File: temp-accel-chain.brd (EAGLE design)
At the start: 29.8 x 10.5 mm, 8 parts, among them U1 ADT7420UCPZ-R2

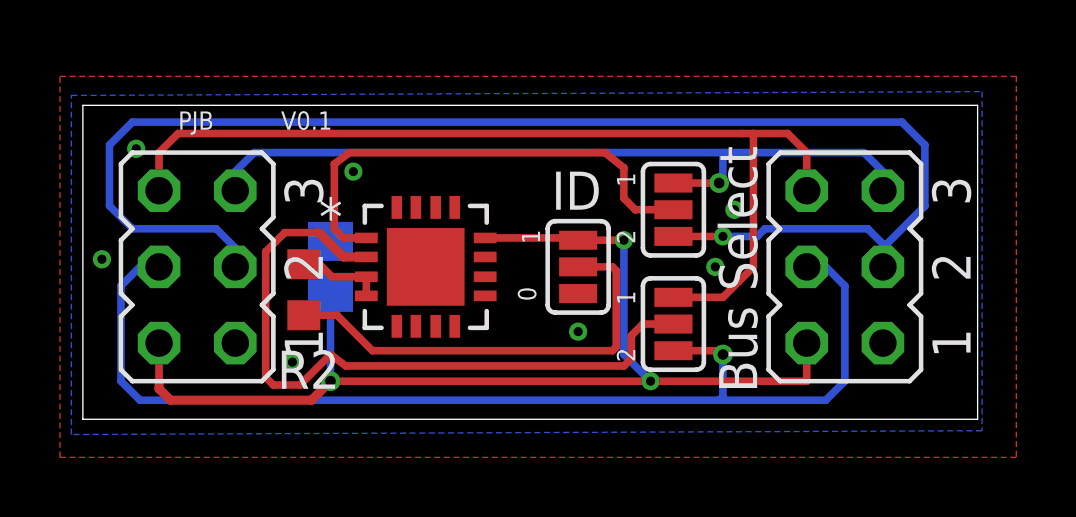
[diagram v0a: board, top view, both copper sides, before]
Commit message: added accel to back and mostly routed
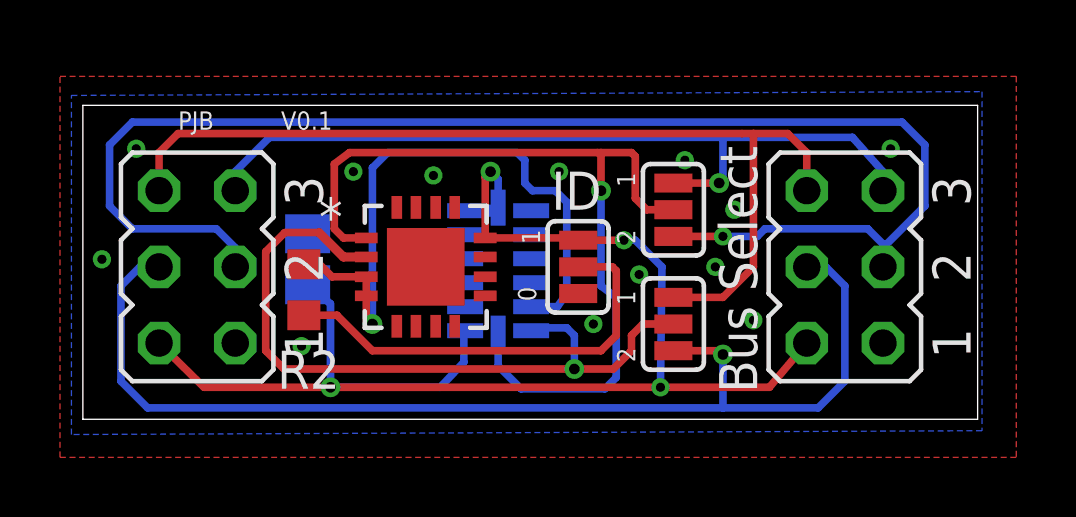
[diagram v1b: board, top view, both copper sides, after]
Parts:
- added U2: ADXL345, SparkFun-Sensors:LGA14
- moved C1 0.80 mm to (8.76, 5.33)
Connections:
- net ADD: now also U2.12
- net GND: now also U2.2, U2.4, U2.5
- net SCL: now also U2.14
- net SDA: now also U2.13
- net VCC: now also U2.1, U2.6, U2.7
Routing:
- net ADD: track 2.89 -> 21.4 mm, vias 0 -> 1
- net SCL: track 16.1 -> 29.6 mm, vias 0 -> 1
- net VCC: track 37.5 -> 47.7 mm, vias 3 -> 4
- net SDA: track 23.4 -> 24.7 mm, vias 0 -> 1
- net SCL1: track 26.0 -> 26.9 mm

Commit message: completely routed board
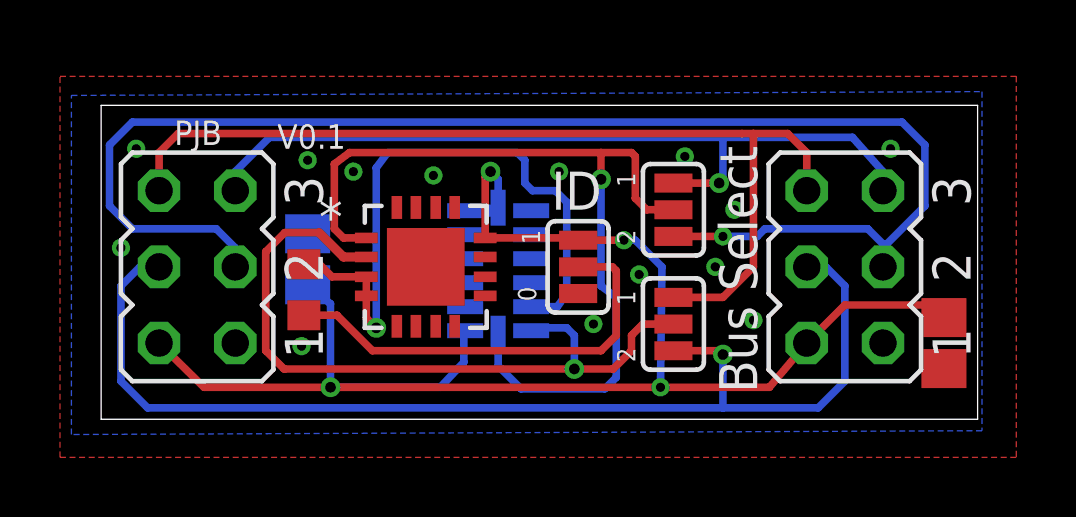
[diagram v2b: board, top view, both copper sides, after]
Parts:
- added C2: (no value), resistor:C0805
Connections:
- net GND: now also C2.2
- net VCC: now also C2.1
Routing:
- net VCC: track 47.7 -> 53.3 mm
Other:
- board size 29.8 x 10.5 mm -> 29.2 x 10.5 mm
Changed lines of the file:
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@@
 <setting verticaltext="up"/>
 </settings>
-<grid distance="5" unitdist="mil" unit="mil" style="lines" multiple="1" display="no" altdistance="1" altunitdist="mil" altunit="mil"/>
+<grid distance="5" unitdist="mil" unit="mm" style="lines" multiple="1" display="no" altdistance="1" altunitdist="mil" altunit="mil"/>
 <layers>
 <layer number="1" name="Top" color="4" fill="1" visible="yes" active="yes"/>
@@
 <layer number="21" name="tPlace" color="7" fill="1" visible="no" active="yes"/>
 <layer number="22" name="bPlace" color="7" fill="1" visible="yes" active="yes"/>
-<layer number="23" name="tOrigins" color="15" fill="1" visible="no" active="yes"/>
+<layer number="23" name="tOrigins" color="15" fill="1" visible="yes" active="yes"/>
 <layer number="24" name="bOrigins" color="15" fill="1" visible="yes" active="yes"/>
-<layer number="25" name="tNames" color="7" fill="1" visible="no" active="yes"/>
+<layer number="25" name="tNames" color="7" fill="1" visible="yes" active="yes"/>
 <layer number="26" name="bNames" color="7" fill="1" visible="yes" active="yes"/>
-<layer number="27" name="tValues" color="7" fill="1" visible="no" active="yes"/>
+<layer number="27" name="tValues" color="7" fill="1" visible="yes" active="yes"/>
 <layer number="28" name="bValues" color="7" fill="1" visible="yes" active="yes"/>
 <layer number="29" name="tStop" color="7" fill="3" visible="no" active="yes"/>
@@
 <board>
 <plain>
-<wire x1="1.27" y1="0" x2="31.095" y2="0" width="0" layer="20"/>
+<wire x1="1.8796" y1="0" x2="31.095" y2="0" width="0" layer="20"/>
 <wire x1="31.095" y1="0" x2="31.095" y2="10.465" width="0" layer="20"/>
-<wire x1="31.095" y1="10.465" x2="1.27" y2="10.465" width="0" layer="20"/>
-<wire x1="1.27" y1="10.465" x2="1.27" y2="0" width="0" layer="20"/>
+<wire x1="31.095" y1="10.465" x2="1.8796" y2="10.465" width="0" layer="20"/>
+<wire x1="1.8796" y1="10.465" x2="1.8796" y2="0" width="0" layer="20"/>
 <text x="23.749" y="0.889" size="1.27" layer="25" rot="R90">Bus Select</text>
 <text x="19.685" y="3.81" size="0.6096" layer="25" rot="R90">1</text>
@@
 <text x="16.383" y="3.937" size="0.6096" layer="25" rot="R90">0</text>
 <text x="16.51" y="5.842" size="0.6096" layer="25" rot="R90">1</text>
-<text x="4.445" y="9.652" size="0.6096" layer="25">PJB</text>
-<text x="7.874" y="9.652" size="0.6096" layer="25">V0.1</text>
+<text x="4.318" y="9.144" size="0.8128" layer="25">PJB</text>
+<text x="7.747" y="9.017" size="0.8128" layer="25">V0.1</text>
 </plain>
 <attributes>
@@
 <attribute name="VALUE" x="17.78" y="4.9799" size="0.02" layer="27" rot="R90"/>
 </element>
-<element name="R2" library="resistor" package="R0603" value="10K" x="8.636" y="4.318" smashed="yes" rot="R90">
-<attribute name="NAME" x="7.747" y="1.016" size="1.27" layer="25"/>
+<element name="R2" library="resistor" package="R0603" value="10K" x="8.636" y="4.318" smashed="yes" rot="R90"/>
+<element name="U2" library="SparkFun-Sensors" package="LGA14" value="ADXL345" x="15.113" y="4.953" smashed="yes" rot="MR270"/>
+<element name="C2" library="resistor" package="C0805" value="" x="29.972" y="2.54" smashed="yes" rot="R270">
+<attribute name="VALUE" x="27.686" y="3.429" size="1.27" layer="27" rot="R270"/>
 </element>
-<element name="U2" library="SparkFun-Sensors" package="LGA14" value="ADXL345" x="15.113" y="4.953" smashed="yes" rot="MR270"/>
 </elements>
 <signals>
@@
 <wire x1="9.525" y1="1.0668" x2="9.525" y2="3.849" width="0.254" layer="16"/>
 <wire x1="9.525" y1="3.849" x2="8.763" y2="4.484" width="0.254" layer="16"/>
+<contactref element="C2" pad="1"/>
+<wire x1="29.972" y1="3.39" x2="29.972" y2="3.175" width="0.254" layer="1"/>
+<wire x1="29.972" y1="3.175" x2="29.337" y2="3.81" width="0.254" layer="1"/>
+<wire x1="29.337" y1="3.81" x2="26.67" y2="3.81" width="0.254" layer="1"/>
+<wire x1="26.67" y1="3.81" x2="25.4" y2="2.54" width="0.254" layer="1"/>
 </signal>
 <signal name="SCL1">
@@
 <vertex x="0.889" y="-0.508"/>
 </polygon>
-<via x="18.288" y="3.175" extent="1-16" drill="0.3048" diameter="0.508"/>
 <via x="22.352" y="5.08" extent="1-16" drill="0.3048" diameter="0.508"/>
 <via x="8.5598" y="2.4384" extent="1-16" drill="0.3048" diameter="0.508"/>
-<via x="1.905" y="5.334" extent="1-16" drill="0.3048" diameter="0.508"/>
+<via x="2.54" y="5.715" extent="1-16" drill="0.3048" diameter="0.508"/>
 <via x="10.287" y="8.255" extent="1-16" drill="0.3048" diameter="0.508"/>
 <via x="3.048" y="9.017" extent="1-16" drill="0.3048" diameter="0.508"/>
@@
 <via x="19.812" y="4.826" extent="1-16" drill="0.3048" diameter="0.508"/>
 <via x="23.622" y="3.302" extent="1-16" drill="0.3048" diameter="0.508"/>
-<via x="21.336" y="8.636" extent="1-16" drill="0.3048" diameter="0.508"/>
-<wire x1="14.6812" y1="5.4102" x2="14.013" y2="5.353" width="0" layer="19" extent="1-16"/>
+<via x="21.336" y="8.763" extent="1-16" drill="0.3048" diameter="0.508"/>
+<contactref element="C2" pad="2"/>
+<via x="8.763" y="8.636" extent="1-16" drill="0.3048" diameter="0.508"/>
+<via x="18.288" y="3.175" extent="1-16" drill="0.3048" diameter="0.508"/>
 </signal>
 <signal name="SDA">
@@
 <wire x1="9.652" y1="6.35" x2="9.652" y2="8.509" width="0.254" layer="1"/>
 <wire x1="9.652" y1="8.509" x2="10.16" y2="8.89" width="0.254" layer="1"/>
-<wire x1="10.16" y1="8.89" x2="18.415" y2="8.89" width="0.254" layer="1"/>
+<wire x1="10.16" y1="8.89" x2="18.542" y2="8.89" width="0.254" layer="1"/>
 <contactref element="U2" pad="14"/>
 <wire x1="18.542" y1="8.89" x2="19.558" y2="8.89" width="0.254" layer="1"/>
@@
 <wire x1="19.05" y1="1.397" x2="19.05" y2="4.064" width="0.254" layer="16"/>
 <wire x1="19.05" y1="4.064" x2="18.542" y2="4.445" width="0.254" layer="16"/>
-<wire x1="18.542" y1="4.445" x2="18.542" y2="7.62" width="0.254" layer="16"/>
-<via x="18.542" y="7.62" extent="1-16" drill="0.3556" diameter="0.508"/>
+<wire x1="18.542" y1="4.445" x2="18.542" y2="8.001" width="0.254" layer="16"/>
+<via x="18.542" y="8.001" extent="1-16" drill="0.3556" diameter="0.508"/>
 <wire x1="20.955" y1="6.985" x2="20.066" y2="6.985" width="0.254" layer="1"/>
 <wire x1="20.066" y1="6.985" x2="19.685" y2="7.366" width="0.254" layer="1"/>
 <wire x1="19.685" y1="7.366" x2="19.685" y2="8.763" width="0.254" layer="1"/>
 <wire x1="19.685" y1="8.763" x2="19.558" y2="8.89" width="0.254" layer="1"/>
-<wire x1="18.542" y1="7.62" x2="18.542" y2="8.89" width="0.254" layer="1"/>
-<wire x1="18.542" y1="8.89" x2="18.415" y2="8.89" width="0.254" layer="1"/>
+<wire x1="18.542" y1="8.001" x2="18.542" y2="8.89" width="0.254" layer="1"/>
 </signal>
 <signal name="ADD">
@@
 <wire x1="16.002" y1="8.636" x2="15.748" y2="8.89" width="0.254" layer="16"/>
 <wire x1="15.748" y1="8.89" x2="11.43" y2="8.89" width="0.254" layer="16"/>
-<wire x1="11.43" y1="8.89" x2="10.922" y2="8.382" width="0.254" layer="16"/>
-<wire x1="10.922" y1="8.382" x2="10.922" y2="3.175" width="0.254" layer="16"/>
-<via x="10.922" y="3.175" extent="1-16" drill="0.3556" diameter="0.508"/>
-<wire x1="10.922" y1="3.175" x2="10.7188" y2="3.3782" width="0.254" layer="1"/>
+<wire x1="11.43" y1="8.89" x2="11.049" y2="8.382" width="0.254" layer="16"/>
+<wire x1="11.049" y1="8.382" x2="11.049" y2="3.048" width="0.254" layer="16"/>
+<via x="11.049" y="3.048" extent="1-16" drill="0.3556" diameter="0.508"/>
+<wire x1="11.049" y1="3.048" x2="10.7188" y2="3.3782" width="0.254" layer="1"/>
 <wire x1="10.7188" y1="3.3782" x2="10.7188" y2="4.1148" width="0.254" layer="1"/>
 </signal>

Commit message: renumbered
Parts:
- JP1, JP2: value (none) -> JUMPER-3SMD; device jumper:JP3Q -> SparkFun-Passives:SJ_3
- JP4, JP5: value JUMPER-3SMD -> (none); device SparkFun-Passives:SJ_3 -> jumper:JP3Q
- moved JP2 16.0 mm to (21.0, 3.17)
- moved JP4 16.0 mm to (5.08, 5.08)
- moved JP1 8.89 mm to (17.8, 5.08)
- moved JP5 8.89 mm to (26.7, 5.08)
- moved JP3 3.81 mm to (21.0, 6.99)
- renumbered R2 to R1
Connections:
- net ADD_SEL: now also JP1.2; no longer JP5.2
- net GND: now also JP4.1; no longer JP2.1
- net SCL: now also JP3.2; no longer JP4.2
- net SCL1: now also JP3.3, JP4.5, JP5.5; no longer JP1.5, JP2.5, JP4.3
- net SCL2: now also JP3.1, JP4.3, JP5.3; no longer JP1.3, JP2.3, JP4.1
- net SDA: now also JP2.2; no longer JP3.2
- net SDA1: now also JP2.3, JP4.6, JP5.6; no longer JP1.6, JP2.6, JP3.3
- net SDA2: now also JP2.1, JP4.4, JP5.4; no longer JP1.4, JP2.4, JP3.1
- net VCC: now also JP1.3, JP4.2, JP5.2; no longer JP1.2, JP2.2, JP5.3
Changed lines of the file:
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@@
 </autorouter>
 <elements>
-<element name="JP1" library="jumper" package="JP3Q" value="" x="26.67" y="5.08" smashed="yes" rot="R90">
+<element name="JP5" library="jumper" package="JP3Q" value="" x="26.67" y="5.08" smashed="yes" rot="R90">
 <attribute name="VALUE" x="32.512" y="1.651" size="1.27" layer="27" ratio="10" rot="R90"/>
 </element>
-<element name="JP2" library="jumper" package="JP3Q" value="" x="5.08" y="5.08" smashed="yes" rot="R90">
+<element name="JP4" library="jumper" package="JP3Q" value="" x="5.08" y="5.08" smashed="yes" rot="R90">
 <attribute name="VALUE" x="10.922" y="1.651" size="1.27" layer="27" ratio="10" rot="R90"/>
 </element>
-<element name="JP3" library="SparkFun-Passives" package="SJ_3" value="JUMPER-3SMD" x="20.955" y="3.175" smashed="yes" rot="R90"/>
-<element name="JP4" library="SparkFun-Passives" package="SJ_3" value="JUMPER-3SMD" x="20.955" y="6.985" smashed="yes" rot="R90">
+<element name="JP2" library="SparkFun-Passives" package="SJ_3" value="JUMPER-3SMD" x="20.955" y="3.175" smashed="yes" rot="R90"/>
+<element name="JP3" library="SparkFun-Passives" package="SJ_3" value="JUMPER-3SMD" x="20.955" y="6.985" smashed="yes" rot="R90">
 <attribute name="VALUE" x="20.955" y="6.8849" size="0.02" layer="27" rot="R90"/>
 </element>
@@
 <attribute name="OC_FARNELL" value="2306581" x="48.26" y="-1.27" size="1.778" layer="27" display="off"/>
 </element>
-<element name="JP5" library="SparkFun-Passives" package="SJ_3" value="JUMPER-3SMD" x="17.78" y="5.08" smashed="yes" rot="R90">
+<element name="JP1" library="SparkFun-Passives" package="SJ_3" value="JUMPER-3SMD" x="17.78" y="5.08" smashed="yes" rot="R90">
 <attribute name="VALUE" x="17.78" y="4.9799" size="0.02" layer="27" rot="R90"/>
 </element>
-<element name="R2" library="resistor" package="R0603" value="10K" x="8.636" y="4.318" smashed="yes" rot="R90"/>
+<element name="R1" library="resistor" package="R0603" value="10K" x="8.636" y="4.318" smashed="yes" rot="R90"/>
 <element name="U2" library="SparkFun-Sensors" package="LGA14" value="ADXL345" x="15.113" y="4.953" smashed="yes" rot="MR270"/>
 <element name="C2" library="resistor" package="C0805" value="" x="29.972" y="2.54" smashed="yes" rot="R270">
@@
 <signals>
 <signal name="SDA1">
-<contactref element="JP2" pad="6"/>
-<contactref element="JP1" pad="6"/>
-<contactref element="JP3" pad="3"/>
+<contactref element="JP4" pad="6"/>
+<contactref element="JP5" pad="6"/>
+<contactref element="JP2" pad="3"/>
 <wire x1="3.81" y1="7.62" x2="3.81" y2="8.89" width="0.254" layer="1"/>
 <wire x1="3.81" y1="8.89" x2="4.445" y2="9.525" width="0.254" layer="1"/>
@@
 </signal>
 <signal name="SDA2">
-<contactref element="JP2" pad="4"/>
-<contactref element="JP1" pad="4"/>
-<contactref element="JP3" pad="1"/>
+<contactref element="JP4" pad="4"/>
+<contactref element="JP5" pad="4"/>
+<contactref element="JP2" pad="1"/>
 <wire x1="3.81" y1="5.08" x2="3.175" y2="5.08" width="0.254" layer="16"/>
 <wire x1="3.175" y1="5.08" x2="2.54" y2="4.445" width="0.254" layer="16"/>
@@
 </signal>
 <signal name="VCC">
-<contactref element="JP2" pad="2"/>
-<contactref element="JP1" pad="2"/>
+<contactref element="JP4" pad="2"/>
+<contactref element="JP5" pad="2"/>
 <contactref element="C1" pad="1"/>
 <contactref element="U1" pad="12"/>
-<contactref element="JP5" pad="3"/>
+<contactref element="JP1" pad="3"/>
 <wire x1="24.1554" y1="1.0668" x2="25.4" y2="2.54" width="0.254" layer="1"/>
 <via x="9.525" y="1.0668" extent="1-16" drill="0.3556" diameter="0.508"/>
@@
 </signal>
 <signal name="SCL1">
-<contactref element="JP2" pad="5"/>
-<contactref element="JP1" pad="5"/>
-<contactref element="JP4" pad="3"/>
+<contactref element="JP4" pad="5"/>
+<contactref element="JP5" pad="5"/>
+<contactref element="JP3" pad="3"/>
 <wire x1="6.35" y1="7.62" x2="6.35" y2="8.255" width="0.254" layer="16"/>
 <wire x1="6.35" y1="8.255" x2="7.493" y2="9.398" width="0.254" layer="16"/>
@@
 </signal>
 <signal name="SCL2">
-<contactref element="JP2" pad="3"/>
-<contactref element="JP1" pad="3"/>
-<contactref element="JP4" pad="1"/>
+<contactref element="JP4" pad="3"/>
+<contactref element="JP5" pad="3"/>
+<contactref element="JP3" pad="1"/>
 <wire x1="20.955" y1="6.096" x2="22.606" y2="6.096" width="0.254" layer="1"/>
 <via x="22.606" y="6.096" extent="1-16" drill="0.3048" diameter="0.508"/>
@@
 </signal>
 <signal name="GND">
-<contactref element="JP2" pad="1"/>
-<contactref element="JP1" pad="1"/>
+<contactref element="JP4" pad="1"/>
+<contactref element="JP5" pad="1"/>
 <contactref element="C1" pad="2"/>
 <contactref element="U1" pad="11"/>
-<contactref element="JP5" pad="1"/>
+<contactref element="JP1" pad="1"/>
 <polygon width="0.4064" layer="1">
 <vertex x="0.508" y="11.43"/>
@@
 </signal>
 <signal name="SDA">
-<contactref element="JP3" pad="2"/>
+<contactref element="JP2" pad="2"/>
 <contactref element="U1" pad="2"/>
 <wire x1="20.955" y1="3.175" x2="19.939" y2="3.175" width="0.254" layer="1"/>
@@
 </signal>
 <signal name="SCL">
-<contactref element="JP4" pad="2"/>
+<contactref element="JP3" pad="2"/>
 <contactref element="U1" pad="1"/>
 <wire x1="10.7188" y1="6.0452" x2="9.9568" y2="6.0452" width="0.254" layer="1"/>
@@
 </signal>
 <signal name="ADD">
-<contactref element="R2" pad="2"/>
+<contactref element="R1" pad="2"/>
 <contactref element="U1" pad="4"/>
 <contactref element="U1" pad="3"/>
@@
 </signal>
 <signal name="ADD_SEL">
-<contactref element="R2" pad="1"/>
-<contactref element="JP5" pad="2"/>
+<contactref element="R1" pad="1"/>
+<contactref element="JP1" pad="2"/>
 <wire x1="17.78" y1="5.08" x2="18.923" y2="5.08" width="0.254" layer="1"/>
 <wire x1="10.922" y1="2.286" x2="18.542" y2="2.286" width="0.254" layer="1"/>
